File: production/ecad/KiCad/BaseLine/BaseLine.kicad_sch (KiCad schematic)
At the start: 0 parts

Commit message: adding heirarchal labels
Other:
- sheet IO ports: added +3.3V, +5V, CLK, DATA_OUTPUT, ENABLE_MUX, GND, MUX_CS_1, MUX_CS_2, PDWN, SCL, SDA, SPEED; removed none
- sheet Rotary Encoder ports: added +3.3V, +5V, CLK_rotaryenc, CS_rotaryenc, DO_rotaryenc, GND; removed none
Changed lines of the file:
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@@
+			)
+		)
+		(pin "DO_rotaryenc" output
+			(at 204.47 106.68 180)
+			(effects
+				(font
+					(size 1.27 1.27)
+				)
+				(justify left)
+			)
+		)
+		(pin "CS_rotaryenc" input
+			(at 204.47 110.49 180)
+			(effects
+				(font
+					(size 1.27 1.27)
+				)
+				(justify left)
+			)
+		)
+		(pin "CLK_rotaryenc" input
+			(at 204.47 114.3 180)
+			(effects
+				(font
+					(size 1.27 1.27)
+				)
+				(justify left)
+			)
+		)
+		(pin "+5V" input
+			(at 227.33 95.25 90)
+			(effects
+				(font
+					(size 1.27 1.27)
+				)
+				(justify right)
+			)
+		)
+		(pin "GND" input
+			(at 231.14 95.25 90)
+			(effects
+				(font
+					(size 1.27 1.27)
+				)
+				(justify right)
+			)
+		)
+		(pin "+3.3V" input
+			(at 223.52 95.25 90)
+			(effects
+				(font
+					(size 1.27 1.27)
+				)
+				(justify right)
 			)
 		)
@@
 			)
 		)
+		(pin "CLK" input
+			(at 45.72 152.4 90)
+			(effects
+				(font
+					(size 1.27 1.27)
+				)
+				(justify right)
+			)
+		)
+		(pin "PDWN" input
+			(at 48.26 152.4 90)
+			(effects
+				(font
+					(size 1.27 1.27)
+				)
+				(justify right)
+			)
+		)
+		(pin "SPEED" input
+			(at 50.8 152.4 90)
+			(effects
+				(font
+					(size 1.27 1.27)
+				)
+				(justify right)
+			)
+		)
+		(pin "MUX_CS_1" input
+			(at 60.96 152.4 90)
+			(effects
+				(font
+					(size 1.27 1.27)
+				)
+				(justify right)
+			)
+		)
+		(pin "MUX_CS_2" input
+			(at 63.5 152.4 90)
+			(effects
+				(font
+					(size 1.27 1.27)
+				)
+				(justify right)
+			)
+		)
+		(pin "ENABLE_MUX" input
+			(at 66.04 152.4 90)
+			(effects
+				(font
+					(size 1.27 1.27)
+				)
+				(justify right)
+			)
+		)
+		(pin "DATA_OUTPUT" output
+			(at 73.66 152.4 90)
+			(effects
+				(font
+					(size 1.27 1.27)
+				)
+				(justify right)
+			)
+		)
+		(pin "SCL" input
+			(at 39.37 176.53 180)
+			(effects
+				(font
+					(size 1.27 1.27)
+				)
+				(justify left)
+			)
+		)
+		(pin "SDA" output
+			(at 39.37 179.07 180)
+			(effects
+				(font
+					(size 1.27 1.27)
+				)
+				(justify left)
+			)
+		)
+		(pin "+5V" input
+			(at 90.17 170.18 0)
+			(effects
+				(font
+					(size 1.27 1.27)
+				)
+				(justify right)
+			)
+		)
+		(pin "+3.3V" input
+			(at 90.17 172.72 0)
+			(effects
+				(font
+					(size 1.27 1.27)
+				)
+				(justify right)
+			)
+		)
+		(pin "GND" input
+			(at 90.17 175.26 0)
+			(effects
+				(font
+					(size 1.27 1.27)
+				)
+				(justify right)
+			)
+		)

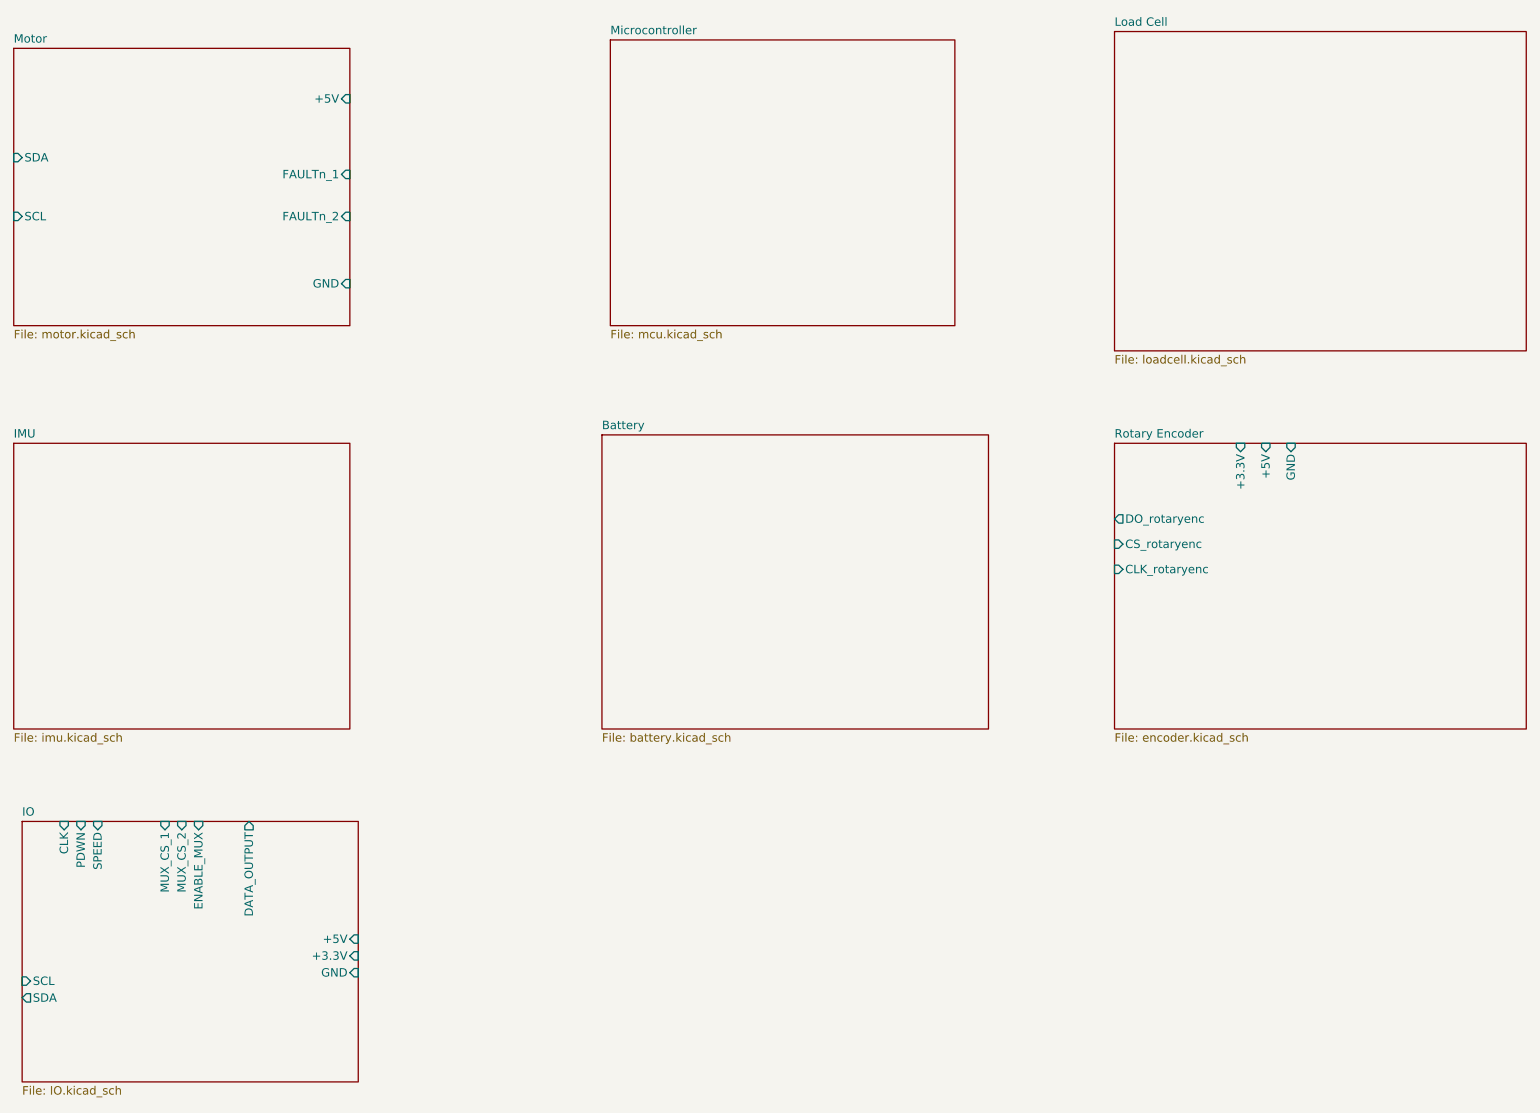
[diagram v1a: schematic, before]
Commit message: Connectors and heirarchal labels
added connectors for power on the Loadcell schem and the battery schem

added the MCU heirarchal labels
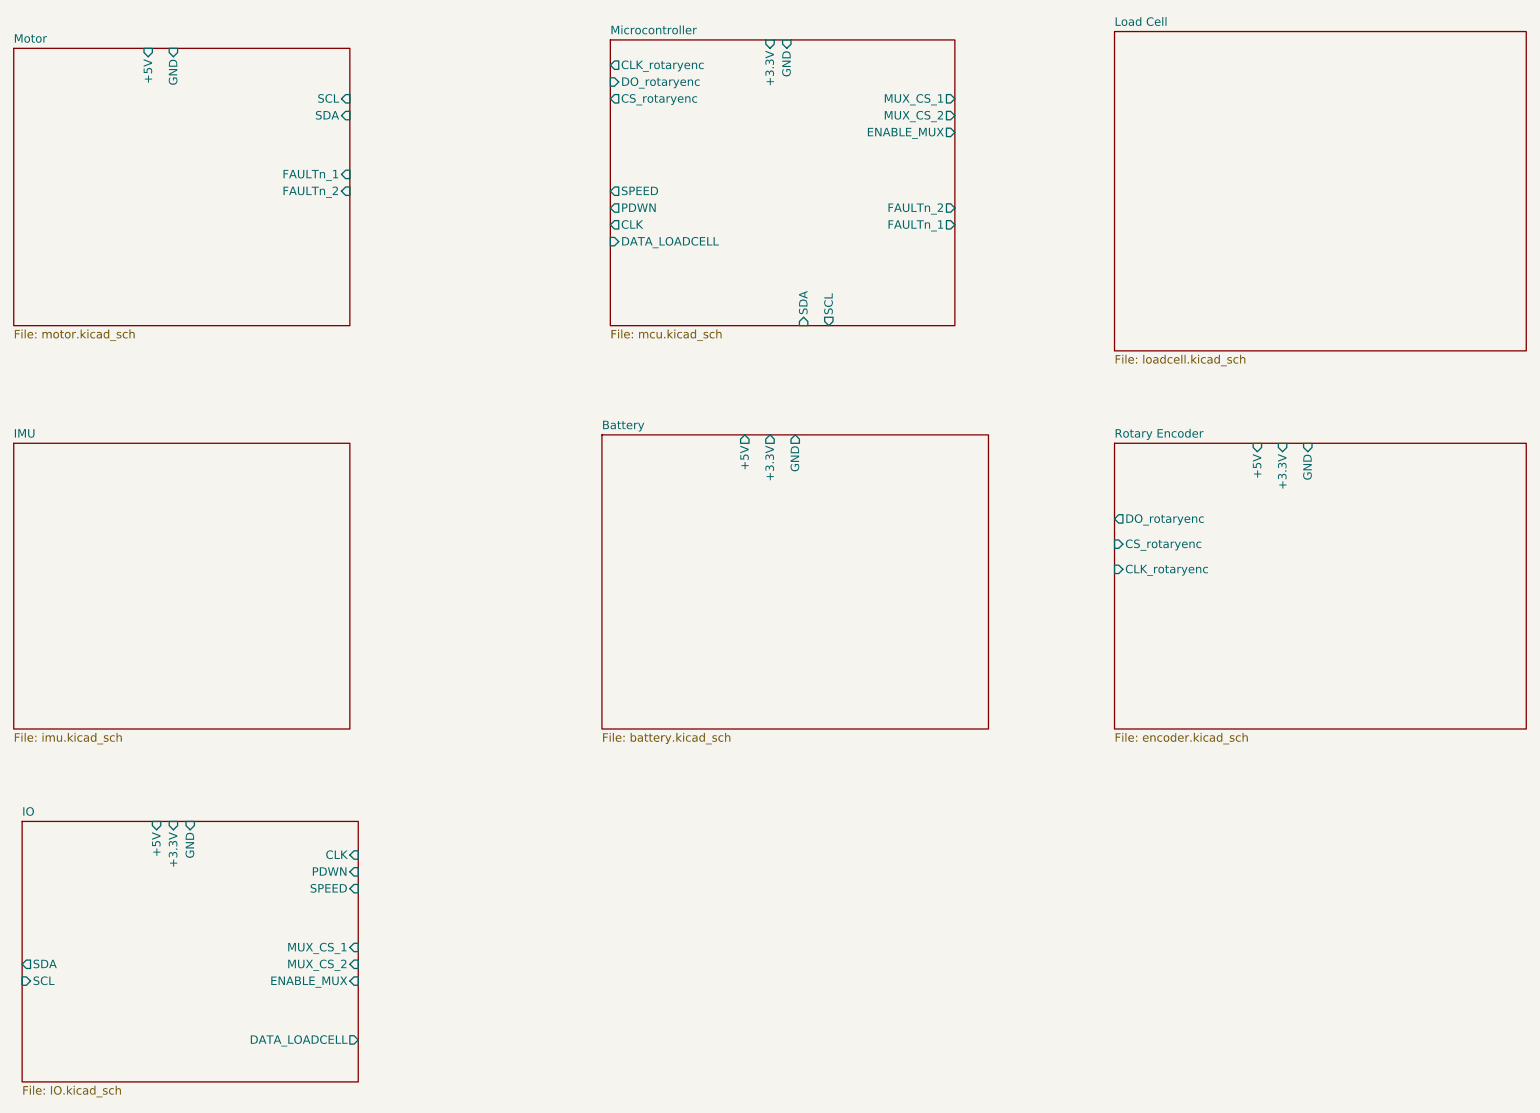
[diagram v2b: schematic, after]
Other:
- sheet Battery ports: added +3.3V, +5V, GND; removed none
- sheet IO ports: added DATA_LOADCELL; removed DATA_OUTPUT
- sheet Microcontroller ports: added +3.3V, CLK, CLK_rotaryenc, CS_rotaryenc, DATA_LOADCELL, DO_rotaryenc, ENABLE_MUX, FAULTn_1, FAULTn_2, GND, MUX_CS_1, MUX_CS_2, PDWN, SCL, SDA, SPEED; removed none
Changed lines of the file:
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@@
+			)
+		)
+		(pin "GND" output
+			(at 156.21 93.98 90)
+			(effects
+				(font
+					(size 1.27 1.27)
+				)
+				(justify right)
+			)
+		)
+		(pin "+3.3V" output
+			(at 152.4 93.98 90)
+			(effects
+				(font
+					(size 1.27 1.27)
+				)
+				(justify right)
+			)
+		)
+		(pin "+5V" output
+			(at 148.59 93.98 90)
+			(effects
+				(font
+					(size 1.27 1.27)
+				)
+				(justify right)
 			)
 		)
@@
 		)
 		(pin "GND" input
-			(at 88.9 71.12 0)
+			(at 62.23 35.56 90)
 			(effects
 				(font
@@
 		)
 		(pin "+5V" input
+			(at 58.42 35.56 90)
+			(effects
+				(font
+					(size 1.27 1.27)
+				)
+				(justify right)
+			)
+		)
+		(pin "SDA" input
+			(at 88.9 45.72 0)
+			(effects
+				(font
+					(size 1.27 1.27)
+				)
+				(justify right)
+			)
+		)
+		(pin "SCL" input
 			(at 88.9 43.18 0)
 			(effects
@@
 				)
 				(justify right)
-			)
-		)
-		(pin "SDA" input
-			(at 38.1 52.07 180)
-			(effects
-				(font
-					(size 1.27 1.27)
-				)
-				(justify left)
-			)
-		)
-		(pin "SCL" input
-			(at 38.1 60.96 180)
-			(effects
-				(font
-					(size 1.27 1.27)
-				)
-				(justify left)
 			)
 		)
@@
 		)
 		(pin "FAULTn_2" input
-			(at 88.9 60.96 0)
+			(at 88.9 57.15 0)
 			(effects
 				(font
@@
 		)
 		(pin "+5V" input
-			(at 227.33 95.25 90)
+			(at 226.06 95.25 90)
 			(effects
 				(font
@@
 		)
 		(pin "GND" input
-			(at 231.14 95.25 90)
+			(at 233.68 95.25 90)
 			(effects
 				(font
@@
 		)
 		(pin "+3.3V" input
-			(at 223.52 95.25 90)
+			(at 229.87 95.25 90)
 			(effects
 				(font
@@
 			)
 		)
+		(pin "CLK_rotaryenc" output
+			(at 128.27 38.1 180)
+			(effects
+				(font
+					(size 1.27 1.27)
+				)
+				(justify left)
+			)
+		)
+		(pin "DO_rotaryenc" input
+			(at 128.27 40.64 180)
+			(effects
+				(font
+					(size 1.27 1.27)
+				)
+				(justify left)
+			)
+		)
+		(pin "CS_rotaryenc" output
+			(at 128.27 43.18 180)
+			(effects
+				(font
+					(size 1.27 1.27)
+				)
+				(justify left)
+			)
+		)
+		(pin "PDWN" output
+			(at 128.27 59.69 180)
+			(effects
+				(font
+					(size 1.27 1.27)
+				)
+				(justify left)
+			)
+		)
+		(pin "CLK" output
+			(at 128.27 62.23 180)
+			(effects
+				(font
+					(size 1.27 1.27)
+				)
+				(justify left)
+			)
+		)
+		(pin "FAULTn_1" output
+			(at 180.34 62.23 0)
+			(effects
+				(font
+					(size 1.27 1.27)
+				)
+				(justify right)
+			)
+		)
+		(pin "SPEED" output
+			(at 128.27 57.15 180)
+			(effects
+				(font
+					(size 1.27 1.27)
+				)
+				(justify left)
+			)
+		)
+		(pin "FAULTn_2" output
+			(at 180.34 59.69 0)
+			(effects
+				(font
+					(size 1.27 1.27)
+				)
+				(justify right)
+			)
+		)
+		(pin "MUX_CS_2" output
+			(at 180.34 45.72 0)
+			(effects
+				(font
+					(size 1.27 1.27)
+				)
+				(justify right)
+			)
+		)
+		(pin "MUX_CS_1" output
+			(at 180.34 43.18 0)
+			(effects
+				(font
+					(size 1.27 1.27)
+				)
+				(justify right)
+			)
+		)
+		(pin "DATA_LOADCELL" input
+			(at 128.27 64.77 180)
+			(effects
+				(font
+					(size 1.27 1.27)
+				)
+				(justify left)
+			)
+		)
+		(pin "ENABLE_MUX" output
+			(at 180.34 48.26 0)
+			(effects
+				(font
+					(size 1.27 1.27)
+				)
+				(justify right)
+			)
+		)
+		(pin "SCL" output
+			(at 161.29 77.47 270)
+			(effects
+				(font
+					(size 1.27 1.27)
+				)
+				(justify left)
+			)
+		)
+		(pin "SDA" input
+			(at 157.48 77.47 270)
+			(effects
+				(font
+					(size 1.27 1.27)
+				)
+				(justify left)
+			)
+		)
+		(pin "+3.3V" input
+			(at 152.4 34.29 90)
+			(effects
+				(font
+					(size 1.27 1.27)
+				)
+				(justify right)
+			)
+		)
+		(pin "GND" input
+			(at 154.94 34.29 90)
+			(effects
+				(font
+					(size 1.27 1.27)
+				)
+				(justify right)
+			)
+		)
 		(instances
 			(project "BaseLine"
@@
 		)
 		(pin "CLK" input
-			(at 45.72 152.4 90)
+			(at 90.17 157.48 0)
 			(effects
 				(font
@@
 		)
 		(pin "PDWN" input
-			(at 48.26 152.4 90)
+			(at 90.17 160.02 0)
 			(effects
 				(font
@@
 		)
 		(pin "SPEED" input
-			(at 50.8 152.4 90)
+			(at 90.17 162.56 0)
 			(effects
 				(font
@@
 		)
 		(pin "MUX_CS_1" input
-			(at 60.96 152.4 90)
+			(at 90.17 171.45 0)
 			(effects
 				(font
@@
 		)
 		(pin "MUX_CS_2" input
-			(at 63.5 152.4 90)
+			(at 90.17 173.99 0)
 			(effects
 				(font
@@
 		)
 		(pin "ENABLE_MUX" input
-			(at 66.04 152.4 90)
-			(effects
-				(font
-					(size 1.27 1.27)
-				)
-				(justify right)
-			)
-		)
-		(pin "DATA_OUTPUT" output
-			(at 73.66 152.4 90)
+			(at 90.17 176.53 0)
 			(effects
 				(font
@@
 		)
 		(pin "SDA" output
-			(at 39.37 179.07 180)
+			(at 39.37 173.99 180)
 			(effects
 				(font
@@
 		)
 		(pin "+5V" input
-			(at 90.17 170.18 0)
+			(at 59.69 152.4 90)
 			(effects
 				(font
@@
 		)
 		(pin "+3.3V" input
-			(at 90.17 172.72 0)
+			(at 62.23 152.4 90)
 			(effects
 				(font
@@
 		)
 		(pin "GND" input
-			(at 90.17 175.26 0)
-			(effects
-				(font
+			(at 64.77 152.4 90)
+			(effects
+				(font
+					(size 1.27 1.27)
+				)
+				(justify right)
+			)
+		)
+		(pin "DATA_LOADCELL" output
+			(at 90.17 185.42 0)
+			(effects
+				(font
